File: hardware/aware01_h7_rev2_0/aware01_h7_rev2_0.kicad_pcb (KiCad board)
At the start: 4 copper layers, 46 x 110 mm, 141 parts, among them IC1 TLV320AIC3204IRHBR, IC2 587-2054-127F, IC3 587-2054-127F, IC4 587-2054-127F, IC5 587-2054-127F, J1 CV3_IN, J10 CV2_IN, J11 V/OCT_IN, J12 CV1_IN, J13 GATE3_IN, J14 GATE4_IN, J2 Conn_02x07_Odd_Even, J3 Conn_02x05_Odd_Even, J4 InL, J5 InR, J6 OutL, J7 OutR, J8 GATE1_IN, J9 GATE2_IN, Q1 MMBT3904, Q2 MMBT3904, Q3 MMBT3904, Q4 MMBT3904, SW1 SW_Push, SW2 SW_Push, SW3 SW_Push, U10 NE5532DRG4, U11 LMV722IDR, U12 LMV722IDR, U2 STM32H7A3RITx, U3 10k, U4 10k, U5 10k, U6 10k, U7 LM1117MP-3.3, U8 LM4040DIM3X-10, U9 NE5532DRG4, Y2 WE-XTAL 24.0MHz 50ppm

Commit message: routing and placement
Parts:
- moved J1 33.0 mm to (186.2, 118.0)
- moved J11 33.0 mm to (153.2, 118.0)
- moved J14 33.0 mm to (186.2, 133.8)
- moved J4 33.0 mm to (153.2, 136.8)
- moved J7 33.0 mm to (186.2, 136.8)
- moved J8 33.0 mm to (153.2, 133.8)
- moved J10 11.0 mm to (175.2, 118.0)
- moved J12 11.0 mm to (164.2, 118.0)
- moved J13 11.0 mm to (175.2, 133.8)
- moved J5 11.0 mm to (164.2, 136.8)
- moved J6 11.0 mm to (175.2, 136.8)
- moved J9 11.0 mm to (164.2, 133.8)
- moved R65 5.90 mm to (167.7, 127.1), turned to -90 degrees
- moved R79 5.77 mm to (178.6, 127.0), turned to -90 degrees
- moved R66 5.61 mm to (173.0, 108.3)
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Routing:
- net /GATE1_IN: track 5.79 -> 78.8 mm, vias 0 -> 2
- net /GATE2_IN: track 6.42 -> 66.1 mm, vias 0 -> 2
- net /Audio Codec/Input Output Channels/INL: track 0.00 -> 54.2 mm, vias 0 -> 2
- net /GATE4_IN: track 7.50 -> 59.6 mm
- net AREF-10: track 4.08 -> 55.6 mm, vias 0 -> 4
- net /GATE3_IN: track 6.95 -> 57.3 mm
- net /Audio Codec/Input Output Channels/INR: track 0.00 -> 46.3 mm, vias 0 -> 2
- net GND: track 94.6 -> 137.8 mm, vias 40 -> 63
- net /FADER4_IN: track 0.00 -> 35.3 mm, vias 0 -> 1
- net /FADER1_IN: track 4.78 -> 30.8 mm
- net Net-(J4-PadT): track 0.00 -> 20.3 mm
- net Net-(C50-Pad1): track 0.00 -> 15.6 mm
- net Net-(C51-Pad1): track 0.00 -> 15.3 mm
- net +3.3V: track 37.3 -> 50.0 mm, vias 19 -> 27
- net Net-(C56-Pad1): track 0.00 -> 11.3 mm
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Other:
- board text added: "J13"
- board text added: "J14"
- board text added: "J8"
- board text added: "J9"
- board text added: "KEEPOUT"

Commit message: further pcb routing
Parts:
- moved R52 0.46 mm to (156.2, 137.9)
- moved R12 0.30 mm to (187.1, 125.2)
- moved C57 0.15 mm to (189.6, 134.7)
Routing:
- net GND: track 137.8 -> 139.0 mm
- net +3.3V: track 50.0 -> 50.9 mm, vias 27 -> 26
- net +12V: track 113.8 -> 112.9 mm
- net Net-(C50-Pad1): track 15.6 -> 15.0 mm
- net Net-(J8-PadT): track 5.34 -> 4.83 mm

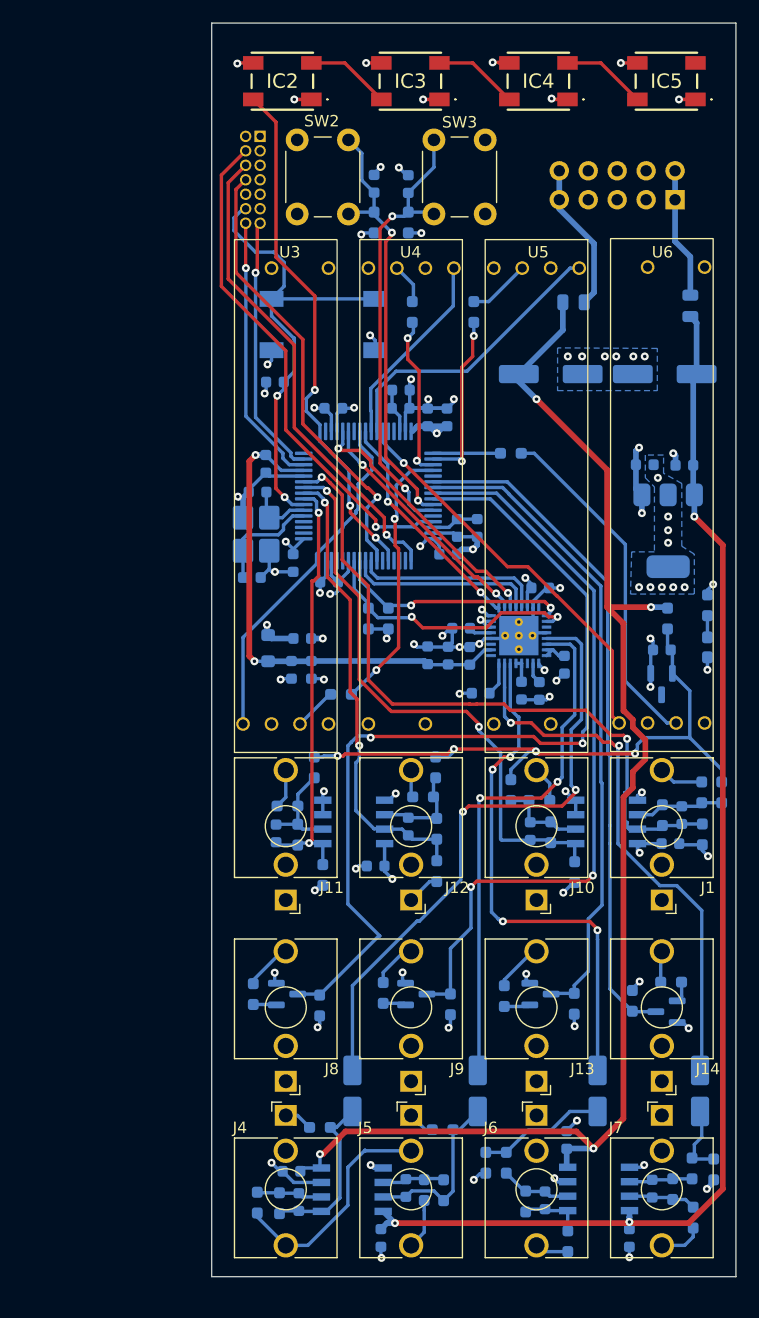
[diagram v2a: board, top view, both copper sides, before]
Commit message: add 5V buck converter
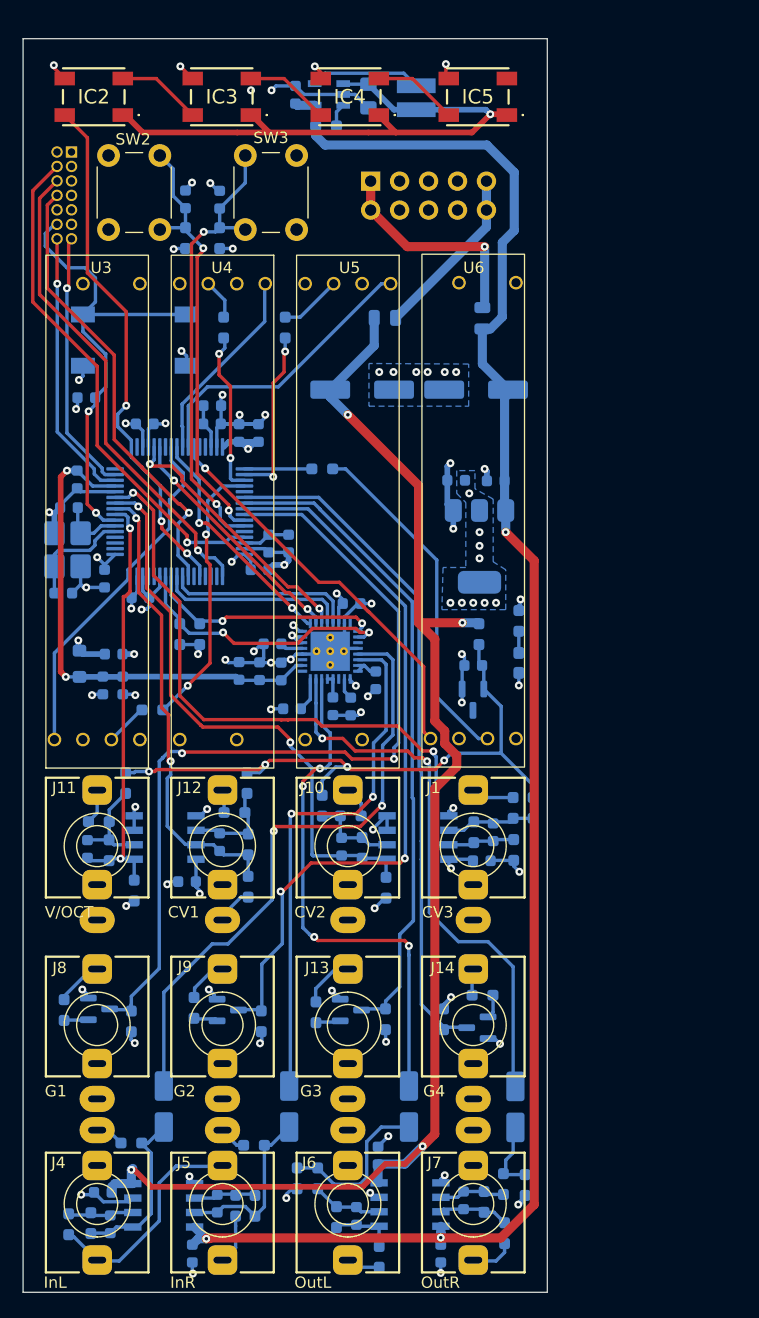
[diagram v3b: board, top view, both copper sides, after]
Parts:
- added C3: 4.7u, Capacitor_SMD:C_0603_1608Metric, B.Cu at (154.1, 47.3)
- added C5: 22u, Capacitor_SMD:C_0805_2012Metric_Pad1.18x1.45mm_HandSolder, B.Cu at (160.5, 47.4)
- added G***: LOGO, LOGO, B.Cu at (150.1, 47.5)
- added IC6: RAA2114054GP3#JA0, Eurorack:RAA2114054GP3#JA0, B.Cu at (157.0, 47.3)
- added L1: 10u, Eurorack:74438335100, B.Cu at (164.7, 47.5)
- added R1: 1M, Resistor_SMD:R_0603_1608Metric_Pad0.98x0.95mm_HandSolder, B.Cu at (156.8, 50.0)
- C1, C2: value 2u2 -> 2.2u
- J1, J10, J11, J12, J13, J14, J4, J5, J6, J7, J8, J9: footprint Connector_Audio:Jack_3.5mm_QingPu_WQP-PJ398SM_Vertical_CircularHoles -> AudioJacks:Jack_3.5mm_QingPu_WQP-PJ398SM_Vertical
- moved J3 26.8 mm to (160.7, 54.9), turned to -90 degrees
- moved J4 18.3 mm to (136.7, 144.6), turned to 180 degrees
- moved J5 18.3 mm to (147.7, 144.6), turned to 180 degrees
- moved J6 18.3 mm to (158.7, 144.6), turned to 180 degrees
- moved J7 18.3 mm to (169.7, 144.6), turned to 180 degrees
- moved D1 18.3 mm to (170.5, 66.9)
- moved J13 17.3 mm to (158.7, 128.9), turned to 0 degrees
- moved J14 17.3 mm to (169.7, 128.9), turned to 0 degrees
- moved J8 17.3 mm to (136.7, 128.9), turned to 0 degrees
- moved J9 17.3 mm to (147.7, 128.9), turned to 0 degrees
- moved J1 17.2 mm to (169.7, 113.2), turned to 0 degrees
- moved J10 17.2 mm to (158.7, 113.2), turned to 0 degrees
- moved J11 17.2 mm to (136.7, 113.2), turned to 0 degrees
- moved J12 17.2 mm to (147.7, 113.2), turned to 0 degrees
- moved Q3 16.7 mm to (159.0, 127.6)
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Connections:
- IC2 pad 1: +3.3V -> +5V
- IC3 pad 1: +3.3V -> +5V
- IC4 pad 1: +3.3V -> +5V
- IC5 pad 1: +3.3V -> +5V
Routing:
- net +5V: track 0.00 -> 53.7 mm, vias 0 -> 1
- net +12V: track 112.9 -> 152.3 mm
- net Net-(IC6-SW): track 0.00 -> 9.75 mm
- net GND: track 139.0 -> 148.1 mm, vias 63 -> 65
- net Net-(D1-A): track 11.5 -> 19.3 mm, vias 0 -> 1
- net +3.3V: track 50.9 -> 43.2 mm, vias 26 -> 22
- net Net-(C56-Pad1): track 11.3 -> 14.3 mm
- net -12V: track 120.6 -> 123.2 mm
- net Net-(D2-K): track 13.2 -> 15.3 mm
- net Net-(IC6-EN): track 0.00 -> 2.04 mm
- net /GATE1_IN: track 78.9 -> 77.1 mm
- net /GATE2_IN: track 66.1 -> 65.2 mm
- net Net-(J4-PadT): track 20.3 -> 19.8 mm
- net /CV3_IN: track 61.3 -> 60.7 mm
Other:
- board text added: "-12V"
- board text added: "Aware Modular Aarebot Rev2.1"
- board text added: "CV1"
- board text added: "CV2"
- board text added: "CV3"
- board text added: "G1"
- board text added: "G2"
- board text added: "G3"
- board text added: "G4"
- board text added: "InL"
- board text added: "InR"
- board text added: "OutL"
- board text added: "OutR"
- board text added: "V/OCT"

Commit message: schematic formatting
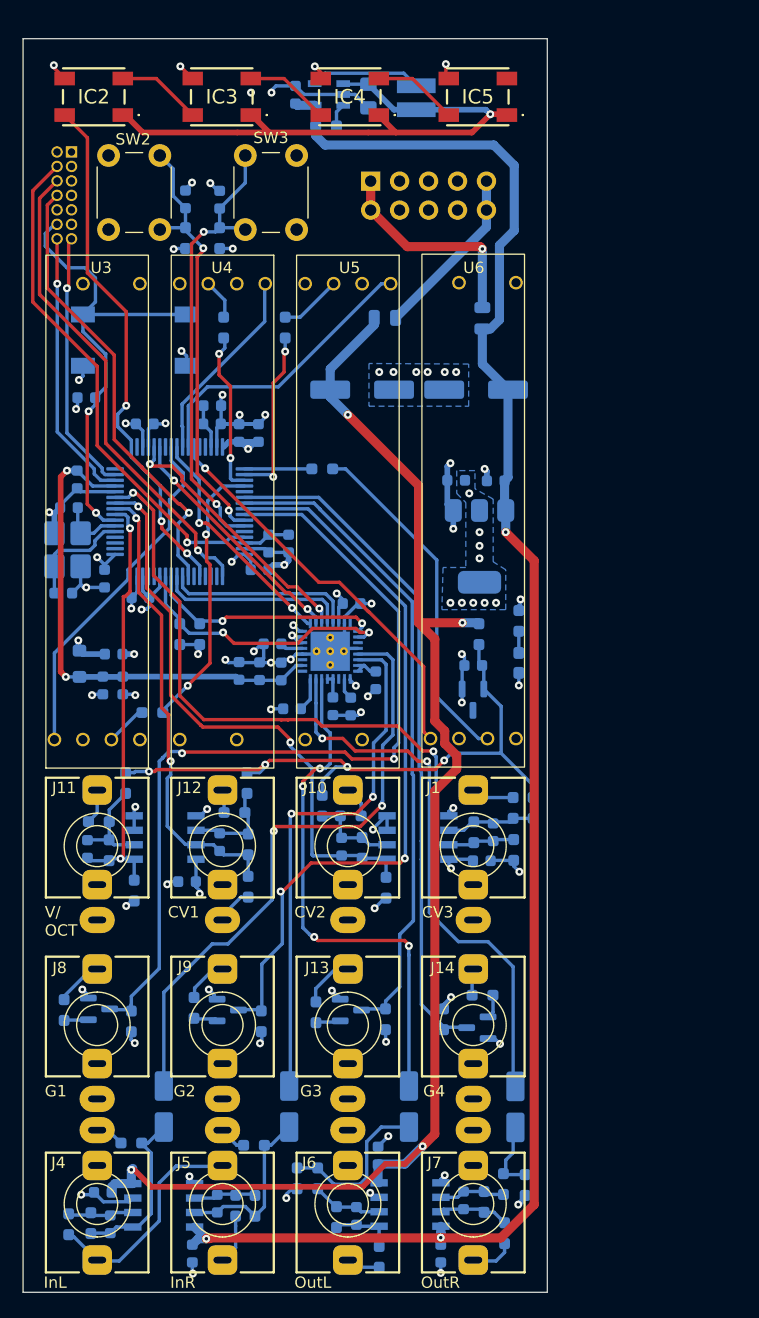
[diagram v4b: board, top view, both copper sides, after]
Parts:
- moved G*** 0.23 mm to (150.1, 47.7)
- moved R42 0.23 mm to (141.6, 101.5)
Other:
- board text added: "Aware Modular Aarebot Rev2"
- board text added: "V/ OCT"
- board text removed: "Aware Modular Aarebot Rev2.1"
- board text removed: "V/OCT"

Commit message: update pcb with 5V buck converter
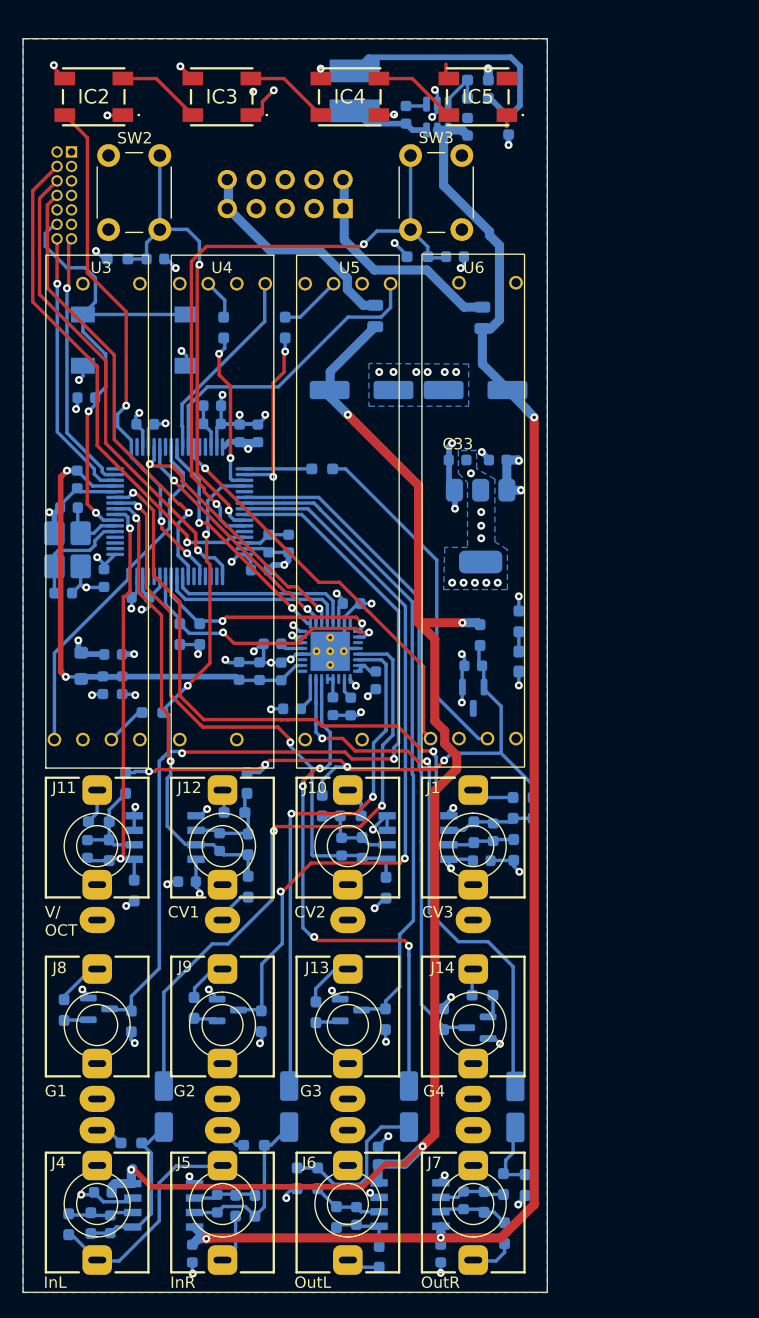
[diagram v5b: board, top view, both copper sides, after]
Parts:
- removed C3: 4.7u, Capacitor_SMD:C_0603_1608Metric
- removed C5: 22u, Capacitor_SMD:C_0805_2012Metric_Pad1.18x1.45mm_HandSolder
- removed IC6: RAA2114054GP3#JA0, Eurorack:RAA2114054GP3#JA0
- removed L1: 10u, Eurorack:74438335100
- removed R1: 1M, Resistor_SMD:R_0603_1608Metric_Pad0.98x0.95mm_HandSolder
- added C25: 10u, Capacitor_SMD:C_0603_1608Metric, B.Cu at (172.8, 50.0)
- added C6: 2.2u, Capacitor_SMD:C_0603_1608Metric, B.Cu at (169.2, 50.1)
- added C7: 100n, Capacitor_SMD:C_0603_1608Metric, B.Cu at (163.8, 49.0)
- added L2: 4.7u, Eurorack:SRR5228A, B.Cu at (159.3, 47.0)
- added R2: 22.1k, Resistor_SMD:R_0603_1608Metric_Pad0.98x0.95mm_HandSolder, B.Cu at (170.1, 46.0)
- added R3: 88.7k, Resistor_SMD:R_0603_1608Metric_Pad0.98x0.95mm_HandSolder, B.Cu at (170.1, 47.6)
- added U1: LMR50410Y5FQDBVRQ1, Package_TO_SOT_SMD:SOT-23-6, B.Cu at (166.6, 49.2)
- moved C17 21.2 mm to (168.1, 61.5), turned to 0 degrees
- moved R41 17.4 mm to (164.8, 61.5), turned to 0 degrees
- moved SW3 14.5 mm to (168.7, 52.6)
- moved R40 6.24 mm to (138.5, 61.7), turned to 0 degrees
- moved C16 5.86 mm to (141.8, 61.7), turned to 0 degrees
- moved J3 3.42 mm to (158.3, 57.3), turned to 90 degrees
- moved C30 1.84 mm to (171.8, 79.3)
- moved C33 1.78 mm to (168.3, 79.3)
- moved U7 1.78 mm to (170.3, 85.1)
- moved D2 0.87 mm to (161.1, 66.7), turned to -90 degrees
- moved G*** 0.28 mm to (150.3, 47.5)
- moved FB1 0.24 mm to (135.3, 97.4)
- moved U8 0.17 mm to (169.7, 100.2)
- moved R47 0.13 mm to (170.3, 94.7)
- moved D3 0.12 mm to (173.7, 97.0)
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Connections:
- C30 pad 1: +12V -> +5V
- U7 pad 3: +12V -> +5V
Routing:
- net +5V: track 53.7 -> 34.9 mm, vias 1 -> 5
- net /BUTTON2_IN: track 40.2 -> 57.7 mm
- net +12V: track 152.7 -> 137.8 mm
- net Net-(IC6-SW): track 9.75 -> 0.00 mm
- net Net-(U1-SW): track 0.00 -> 7.00 mm
- net GND: track 148.3 -> 143.5 mm, vias 65 -> 67
- net Net-(U1-FB): track 0.00 -> 4.42 mm
- net Net-(D2-K): track 15.3 -> 19.5 mm
- net /BUTTON1_IN: track 38.4 -> 41.9 mm
- net Net-(IC6-EN): track 2.04 -> 0.00 mm
- net Net-(U1-CB): track 0.00 -> 1.87 mm
- net /FADER3_IN: track 25.8 -> 27.0 mm
- net Net-(D1-A): track 18.9 -> 19.8 mm, vias 1 -> 0
- net +3.3V: track 43.2 -> 44.0 mm
- net -12V: track 123.2 -> 122.5 mm
- added copper zone on In1.Cu, net +5V

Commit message: refine layout, add testpoints
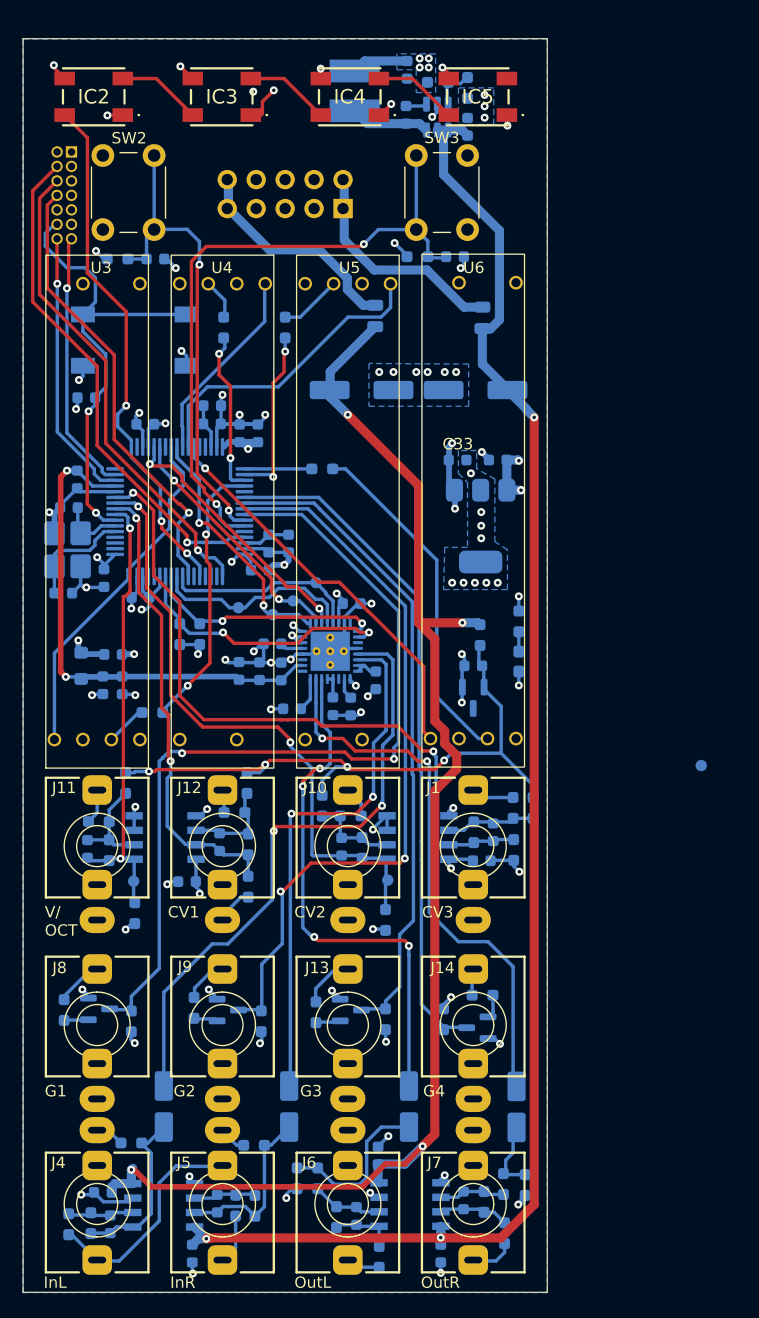
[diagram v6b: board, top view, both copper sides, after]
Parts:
- added TP1: TestPoint, TestPoint:TestPoint_Pad_D1.0mm, B.Cu at (152.1, 92.9)
- added TP10: TestPoint, TestPoint:TestPoint_Pad_D1.0mm, B.Cu at (162.2, 116.2)
- added TP13: TestPoint, TestPoint:TestPoint_Pad_D1.0mm, B.Cu at (139.9, 116.3)
- added TP2: TestPoint, TestPoint:TestPoint_Pad_D1.0mm, B.Cu at (153.9, 91.7)
- added TP3: TestPoint, TestPoint:TestPoint_Pad_D1.0mm, B.Cu at (189.7, 106.2)
- added TP4: TestPoint, TestPoint:TestPoint_Pad_D1.0mm, B.Cu at (149.1, 92.3)
- added TP5: TestPoint, TestPoint:TestPoint_Pad_D1.0mm, B.Cu at (155.9, 90.1)
- moved C25 10.2 mm to (163.9, 45.1)
- moved R3 3.78 mm to (166.6, 46.2), turned to 0 degrees
- moved R69 2.83 mm to (162.0, 119.7)
- moved R76 1.98 mm to (140.0, 119.1)
- moved R2 1.14 mm to (169.2, 46.7), turned to -90 degrees
- moved SW2 0.50 mm to (137.2, 59.1)
- moved SW3 0.50 mm to (169.2, 52.6)
- moved C57 0.10 mm to (173.5, 136.1)
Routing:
- net +5V: track 34.9 -> 17.4 mm, vias 5 -> 10
- net GND: track 143.5 -> 139.7 mm, vias 67 -> 68
- net /CV2_IN: track 51.3 -> 54.1 mm
- net /V_OCT_IN: track 37.8 -> 39.9 mm
- net /I2S1_MCK: track 20.9 -> 22.4 mm
- net /I2S1_SDO: track 16.6 -> 18.0 mm
- net /I2S1_CK: track 21.6 -> 22.3 mm
- net Net-(U1-FB): track 4.42 -> 3.76 mm
- net /I2S1_SDI: track 16.6 -> 17.3 mm
- net /BUTTON2_IN: track 57.7 -> 58.2 mm
- net /BUTTON1_IN: track 41.9 -> 42.4 mm
- added copper zone on B.Cu, net +5V

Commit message: hardware_design: add slide pot filtering
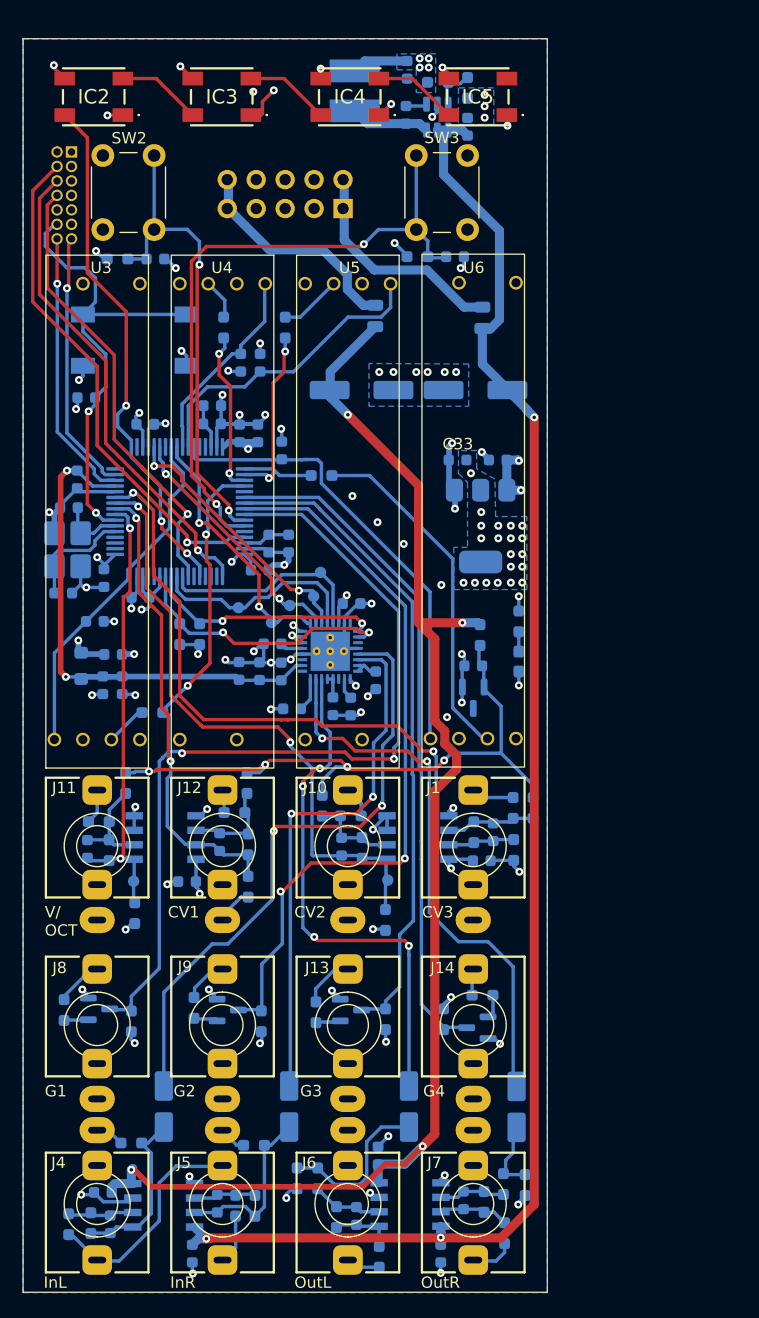
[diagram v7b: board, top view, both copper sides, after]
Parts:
- added C27: 100n, Capacitor_SMD:C_0603_1608Metric, B.Cu at (151.0, 70.8)
- added C28: 100n, Capacitor_SMD:C_0603_1608Metric, B.Cu at (152.9, 78.5)
- added C3: 100n, Capacitor_SMD:C_0603_1608Metric, B.Cu at (136.5, 93.5)
- added C5: 100n, Capacitor_SMD:C_0603_1608Metric, B.Cu at (149.3, 70.8)
- moved TP3 37.1 mm to (155.7, 91.3)
- moved TP5 0.98 mm to (156.3, 89.2)
- moved TP1 0.71 mm to (152.0, 93.6)
- moved R45 0.58 mm to (156.4, 80.7)
- moved TP2 0.50 mm to (153.6, 92.1)
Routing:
- net /FADER4_IN: track 35.3 -> 40.5 mm, vias 1 -> 0
- net GND: track 139.7 -> 143.8 mm, vias 68 -> 77
- net /I2S1_SDI: track 17.3 -> 18.6 mm
- net /I2S1_SDO: track 18.0 -> 19.1 mm
- net /I2S1_MCK: track 22.4 -> 23.1 mm
- net +3.3V: track 44.0 -> 43.8 mm, vias 22 -> 34
- net (no net): vias 5 -> 4
